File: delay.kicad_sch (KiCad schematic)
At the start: 43 parts, among them Q1301 Q_NPN_BEC, Q1302 Q_NPN_BEC, Q1303 Q_NPN_BEC, Q1304 Q_NPN_BEC, U1301 TL072, U1302 MCP6002, U1303 L78L05_SOT89

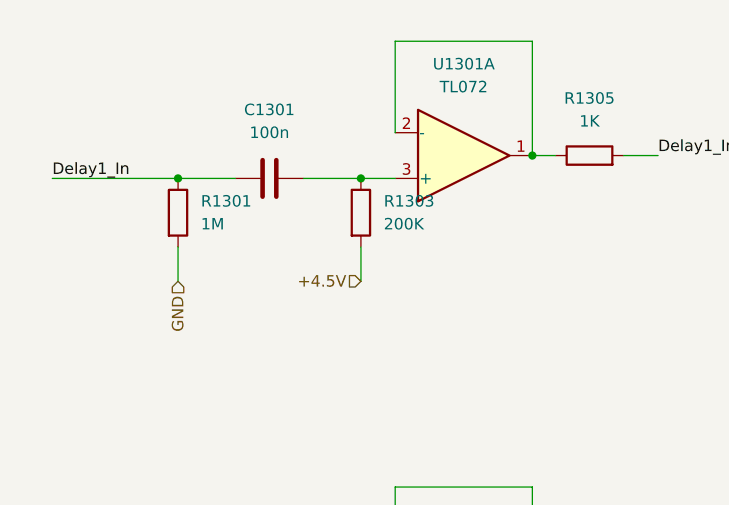
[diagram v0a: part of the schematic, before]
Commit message: Delay layout done
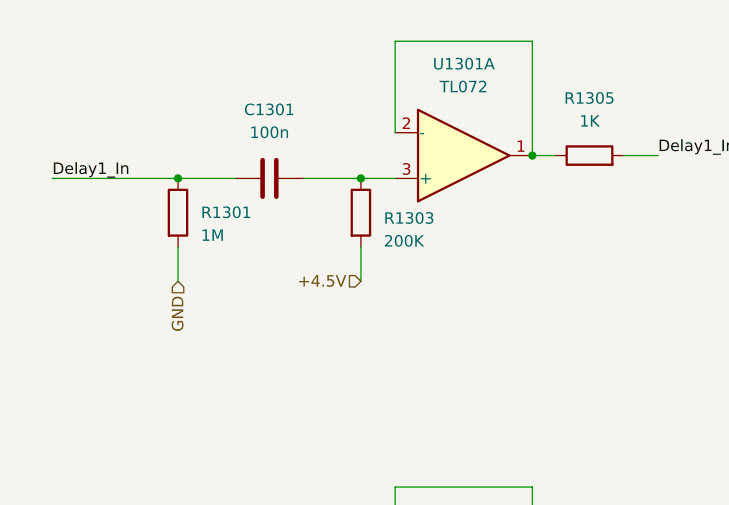
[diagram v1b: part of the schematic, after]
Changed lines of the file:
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@@
   )
   (symbol (lib_id "Device:R") (at 30.48 34.29 0) (unit 1)
-    (in_bom yes) (on_board yes) (fields_autoplaced)
-    (property "Reference" "R1301" (id 0) (at 33.02 33.0199 0)
-      (effects (font (size 1.27 1.27)) (justify left))
-    )
-    (property "Value" "1M" (id 1) (at 33.02 35.5599 0)
+    (in_bom yes) (on_board yes)
+    (property "Reference" "R1301" (id 0) (at 33.02 34.29 0)
+      (effects (font (size 1.27 1.27)) (justify left))
+    )
+    (property "Value" "1M" (id 1) (at 33.02 36.83 0)
       (effects (font (size 1.27 1.27)) (justify left))
     )
@@
   )
   (symbol (lib_id "Device:R") (at 50.8 34.29 0) (unit 1)
-    (in_bom yes) (on_board yes) (fields_autoplaced)
-    (property "Reference" "R1303" (id 0) (at 53.34 33.0199 0)
-      (effects (font (size 1.27 1.27)) (justify left))
-    )
-    (property "Value" "200K" (id 1) (at 53.34 35.5599 0)
-      (effects (font (size 1.27 1.27)) (justify left))
-    )
+    (in_bom yes) (on_board yes)
+    (property "Reference" "R1303" (id 0) (at 53.34 34.925 0)
+      (effects (font (size 1.27 1.27)) (justify left))
+    )
+    (property "Value" "200K" (id 1) (at 53.34 37.465 0)
+      (effects (font (size 1.27 1.27)) (justify left))
+    )

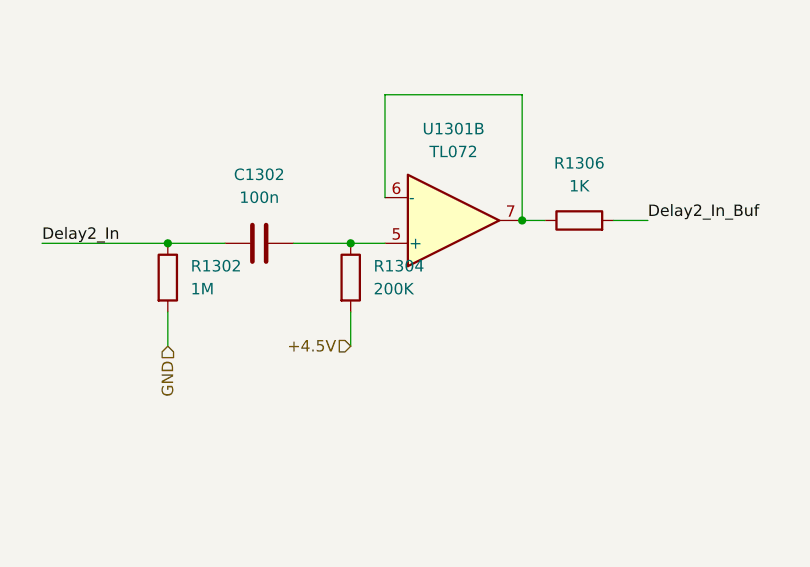
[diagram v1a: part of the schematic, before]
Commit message: Mixer/Crossfader schem capture done
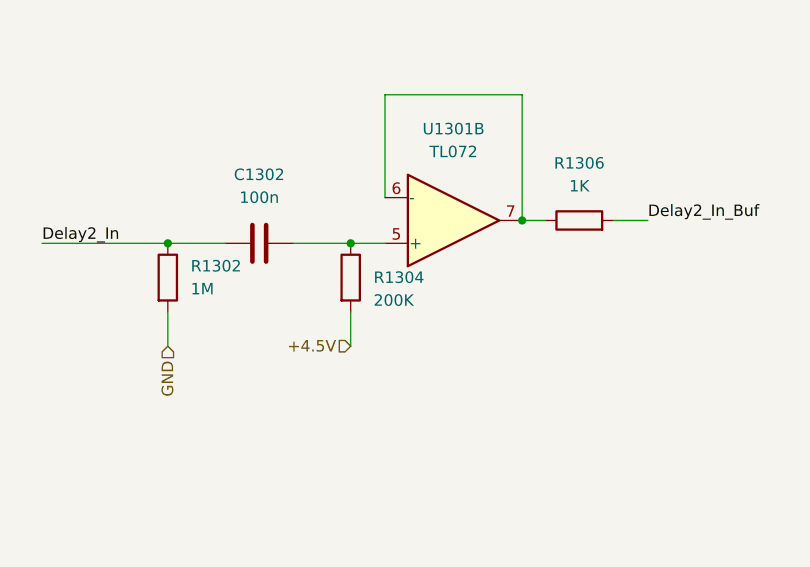
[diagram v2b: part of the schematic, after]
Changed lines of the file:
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@@
   )
   (symbol (lib_id "Device:R") (at 50.8 85.09 0) (unit 1)
-    (in_bom yes) (on_board yes) (fields_autoplaced)
-    (property "Reference" "R1304" (id 0) (at 53.34 83.8199 0)
+    (in_bom yes) (on_board yes)
+    (property "Reference" "R1304" (id 0) (at 53.34 85.09 0)
       (effects (font (size 1.27 1.27)) (justify left))
     )
-    (property "Value" "200K" (id 1) (at 53.34 86.3599 0)
+    (property "Value" "200K" (id 1) (at 53.34 87.63 0)
       (effects (font (size 1.27 1.27)) (justify left))
     )

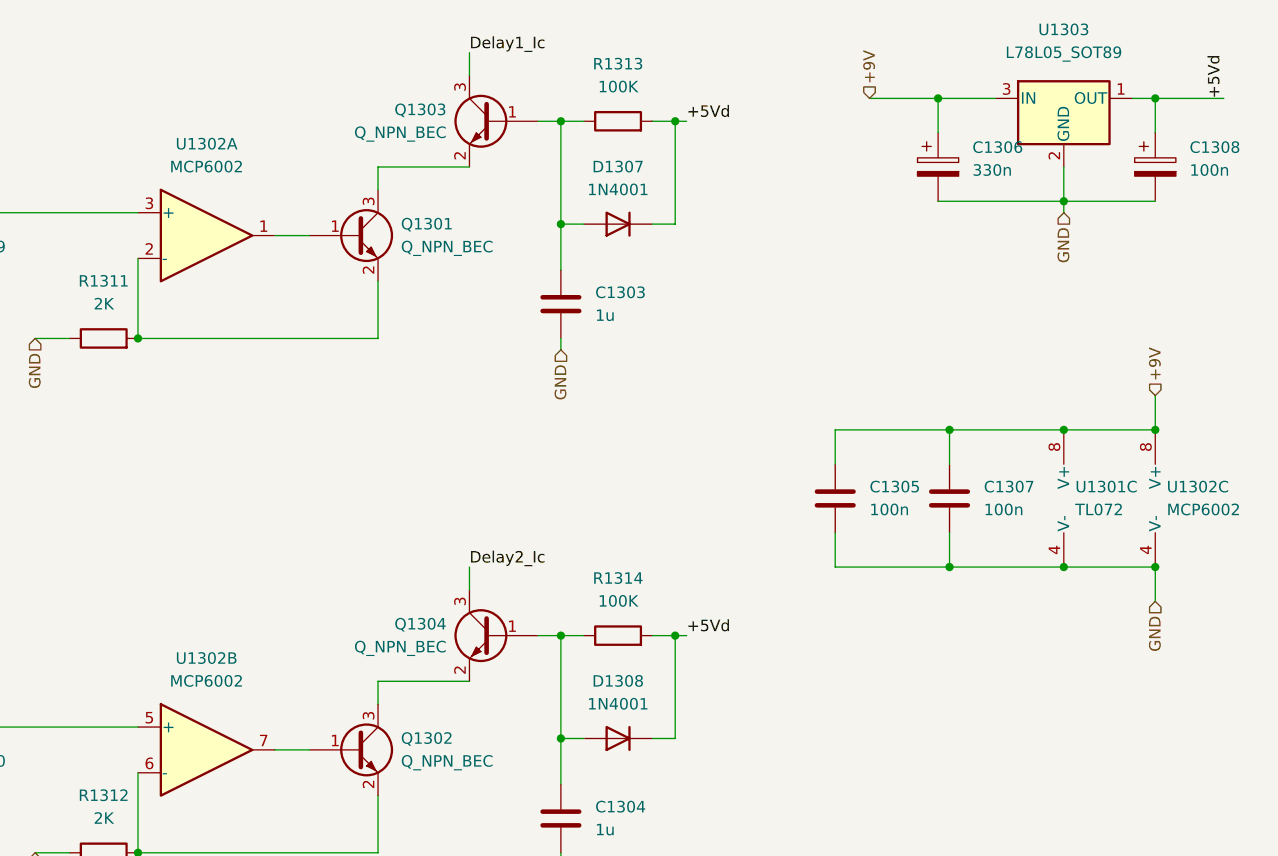
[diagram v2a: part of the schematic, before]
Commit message: LFO schem capture done / replace r2r opamps
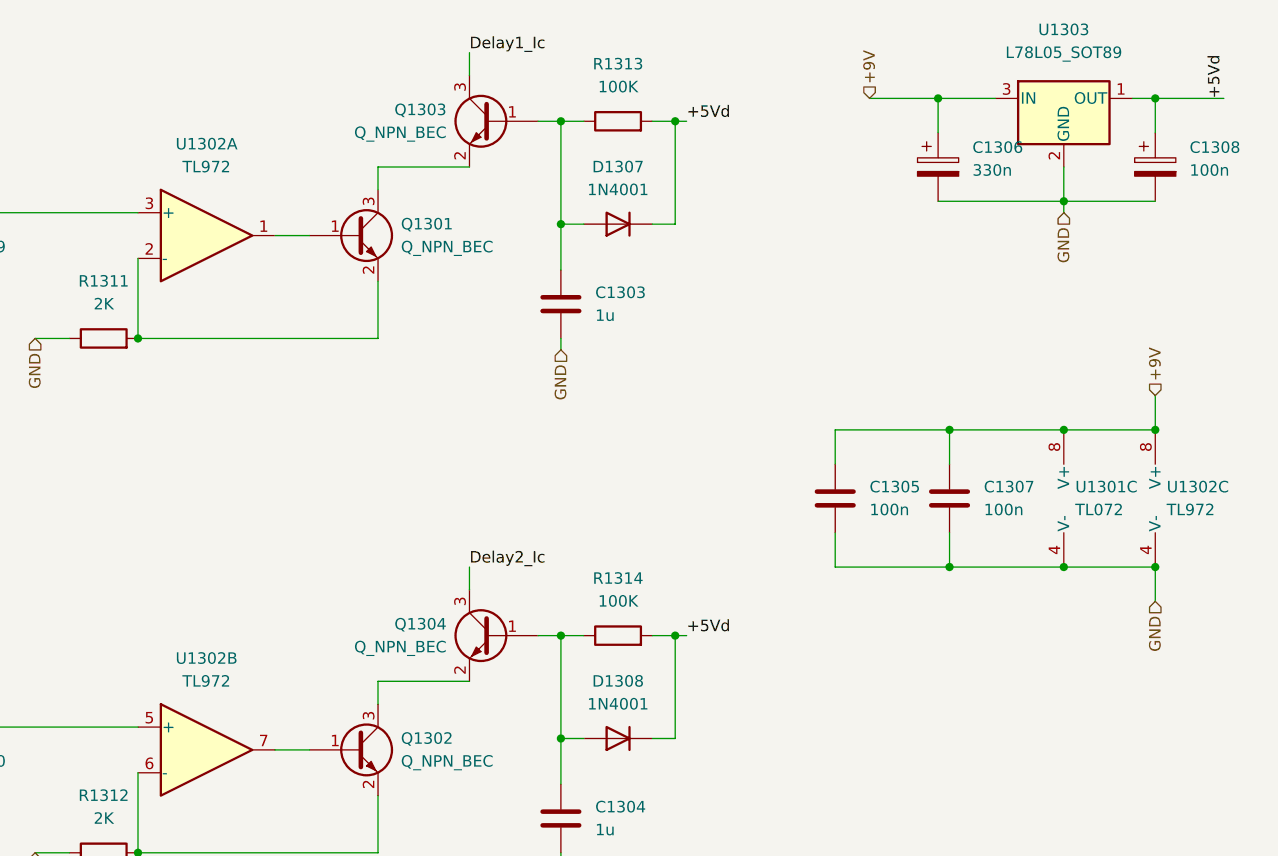
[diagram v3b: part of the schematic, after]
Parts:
- U1302: value MCP6002 -> TL972
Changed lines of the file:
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@@
     (in_bom yes) (on_board yes) (fields_autoplaced)
     (property "Reference" "U1302" (id 0) (at 168.91 26.67 0))
-    (property "Value" "MCP6002" (id 1) (at 168.91 29.21 0))
+    (property "Value" "TL972" (id 1) (at 168.91 29.21 0))
     (property "Footprint" "Package_SO:SOIC-8_3.9x4.9mm_P1.27mm" (id 2) (at 168.91 36.83 0)
       (effects (font (size 1.27 1.27)) hide)
@@
       (effects (font (size 1.27 1.27)) (justify left))
     )
-    (property "Value" "MCP6002" (id 1) (at 275.59 67.3099 0)
+    (property "Value" "TL972" (id 1) (at 275.59 67.3099 0)
       (effects (font (size 1.27 1.27)) (justify left))
     )
@@
     (in_bom yes) (on_board yes) (fields_autoplaced)
     (property "Reference" "U1302" (id 0) (at 168.91 83.82 0))
-    (property "Value" "MCP6002" (id 1) (at 168.91 86.36 0))
+    (property "Value" "TL972" (id 1) (at 168.91 86.36 0))
     (property "Footprint" "Package_SO:SOIC-8_3.9x4.9mm_P1.27mm" (id 2) (at 168.91 93.98 0)
       (effects (font (size 1.27 1.27)) hide)

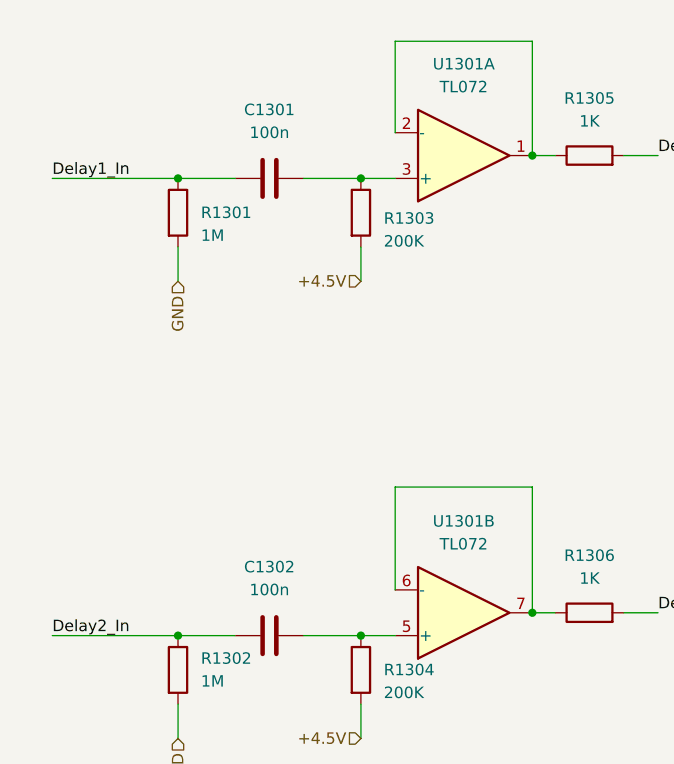
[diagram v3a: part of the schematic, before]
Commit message: Increase the size of dc blocking caps
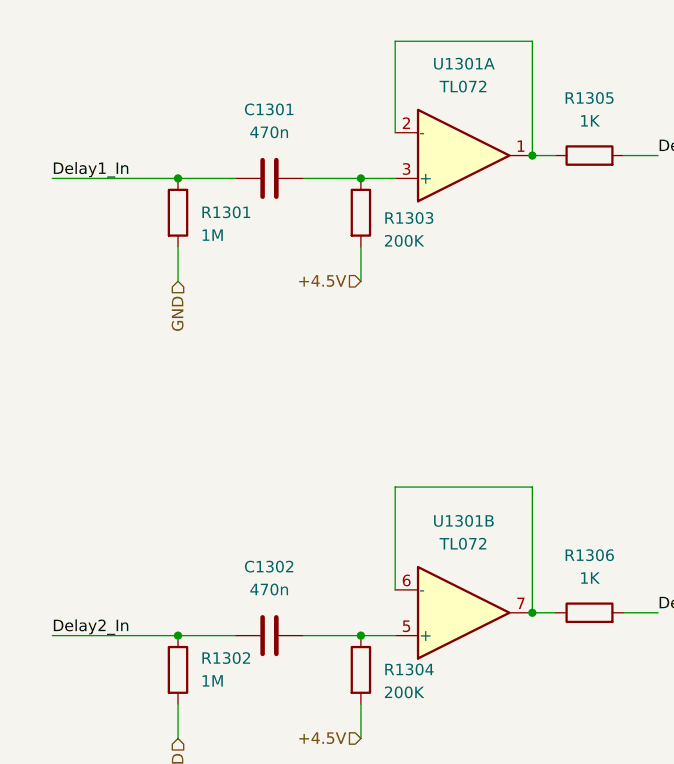
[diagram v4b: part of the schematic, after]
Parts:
- C1301, C1302: value 100n -> 470n; footprint Capacitor_SMD:C_0603_1608Metric_Pad1.08x0.95mm_HandSolder -> Capacitor_SMD:C_0805_2012Metric_Pad1.18x1.45mm_HandSolder
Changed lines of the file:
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@@
+    (pin "2")
+  )
+  (symbol (lib_id "Device:C") (at 40.64 81.28 90) (unit 1)
+    (in_bom yes) (on_board yes) (fields_autoplaced)
+    (property "Reference" "C1302" (id 0) (at 40.64 73.66 90))
+    (property "Value" "470n" (id 1) (at 40.64 76.2 90))
+    (property "Footprint" "Capacitor_SMD:C_0805_2012Metric_Pad1.18x1.45mm_HandSolder" (id 2) (at 44.45 80.3148 0)
+      (effects (font (size 1.27 1.27)) hide)
+    )
+    (property "Datasheet" "~" (id 3) (at 40.64 81.28 0)
+      (effects (font (size 1.27 1.27)) hide)
+    )
+    (pin "1")
     (pin "2")
   )
@@
     (pin "2")
   )
-  (symbol (lib_id "Device:C") (at 40.64 81.28 90) (unit 1)
-    (in_bom yes) (on_board yes) (fields_autoplaced)
-    (property "Reference" "C1302" (id 0) (at 40.64 73.66 90))
-    (property "Value" "100n" (id 1) (at 40.64 76.2 90))
-    (property "Footprint" "Capacitor_SMD:C_0603_1608Metric_Pad1.08x0.95mm_HandSolder" (id 2) (at 44.45 80.3148 0)
-      (effects (font (size 1.27 1.27)) hide)
-    )
-    (property "Datasheet" "~" (id 3) (at 40.64 81.28 0)
-      (effects (font (size 1.27 1.27)) hide)
-    )
-    (pin "1")
-    (pin "2")
-  )
   (symbol (lib_id "Device:R") (at 138.43 39.37 0) (unit 1)
     (in_bom yes) (on_board yes) (fields_autoplaced)
@@
     )
     (property "Datasheet" "~" (id 3) (at 138.43 39.37 0)
+      (effects (font (size 1.27 1.27)) hide)
+    )
+    (pin "1")
+    (pin "2")
+  )
+  (symbol (lib_id "Device:C") (at 40.64 30.48 90) (unit 1)
+    (in_bom yes) (on_board yes) (fields_autoplaced)
+    (property "Reference" "C1301" (id 0) (at 40.64 22.86 90))
+    (property "Value" "470n" (id 1) (at 40.64 25.4 90))
+    (property "Footprint" "Capacitor_SMD:C_0805_2012Metric_Pad1.18x1.45mm_HandSolder" (id 2) (at 44.45 29.5148 0)
+      (effects (font (size 1.27 1.27)) hide)
+    )
+    (property "Datasheet" "~" (id 3) (at 40.64 30.48 0)
       (effects (font (size 1.27 1.27)) hide)
     )
@@
       (effects (font (size 1.27 1.27)) hide)
     )
-    (pin "1")
-    (pin "2")
-  )
-  (symbol (lib_id "Device:C") (at 40.64 30.48 90) (unit 1)
-    (in_bom yes) (on_board yes) (fields_autoplaced)
-    (property "Reference" "C1301" (id 0) (at 40.64 22.86 90))
-    (property "Value" "100n" (id 1) (at 40.64 25.4 90))
-    (property "Footprint" "Capacitor_SMD:C_0603_1608Metric_Pad1.08x0.95mm_HandSolder" (id 2) (at 44.45 29.5148 0)
-      (effects (font (size 1.27 1.27)) hide)
-    )
-    (property "Datasheet" "~" (id 3) (at 40.64 30.48 0)
-      (effects (font (size 1.27 1.27)) hide)
-    )

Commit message: PSU schem update
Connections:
- net +9V: no longer C1306.1, U1303.3 (IN)
- new net +9Vd: C1306.1, U1303.3 (IN)
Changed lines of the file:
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@@
     (effects (font (size 1.27 1.27)) (justify right))
   )
-  (hierarchical_label "+9V" (shape input) (at 242.57 21.59 90)
+  (hierarchical_label "+9Vd" (shape input) (at 242.57 21.59 90)
     (effects (font (size 1.27 1.27)) (justify left))
   )

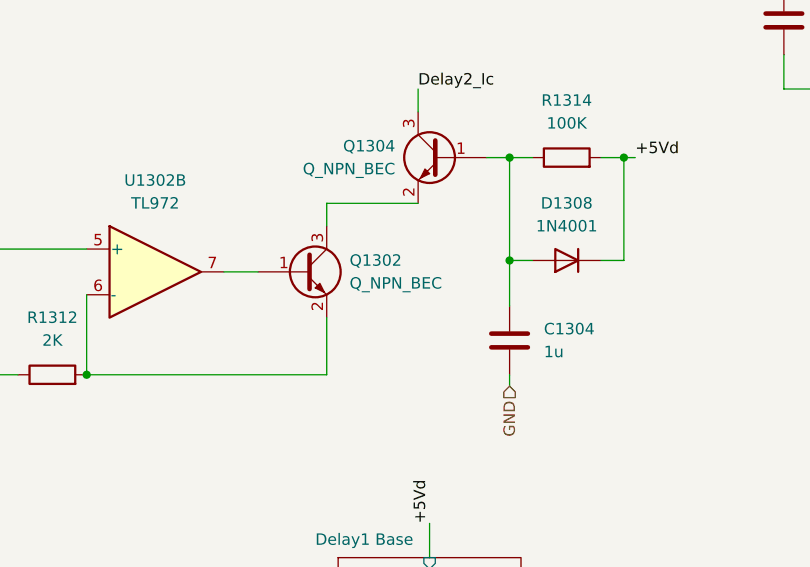
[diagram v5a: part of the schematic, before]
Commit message: Jacks schem done
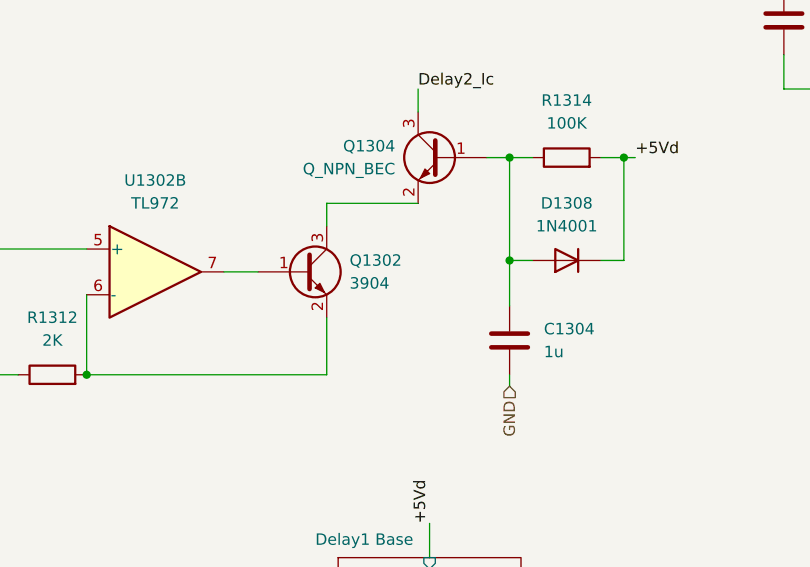
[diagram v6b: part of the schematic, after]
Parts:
- Q1302: value Q_NPN_BEC -> 3904
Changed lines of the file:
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@@
       (effects (font (size 1.27 1.27)) (justify left))
     )
-    (property "Value" "Q_NPN_BEC" (id 1) (at 190.5 95.2499 0)
+    (property "Value" "3904" (id 1) (at 190.5 95.2499 0)
       (effects (font (size 1.27 1.27)) (justify left))
     )

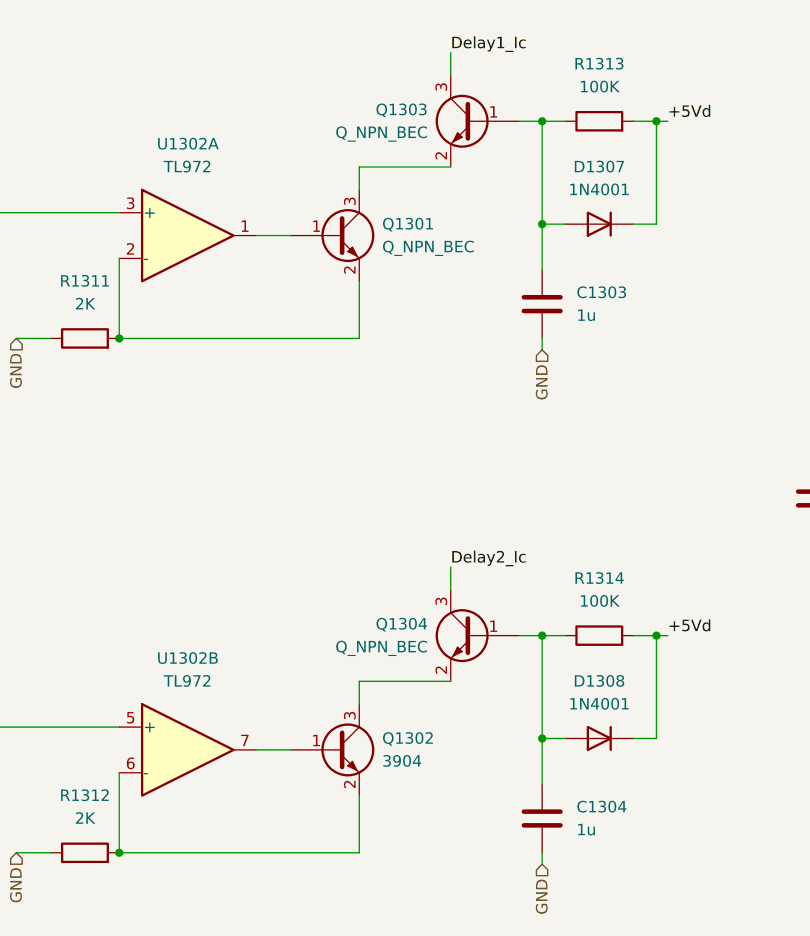
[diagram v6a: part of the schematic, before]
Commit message: Add JLC parts numbers
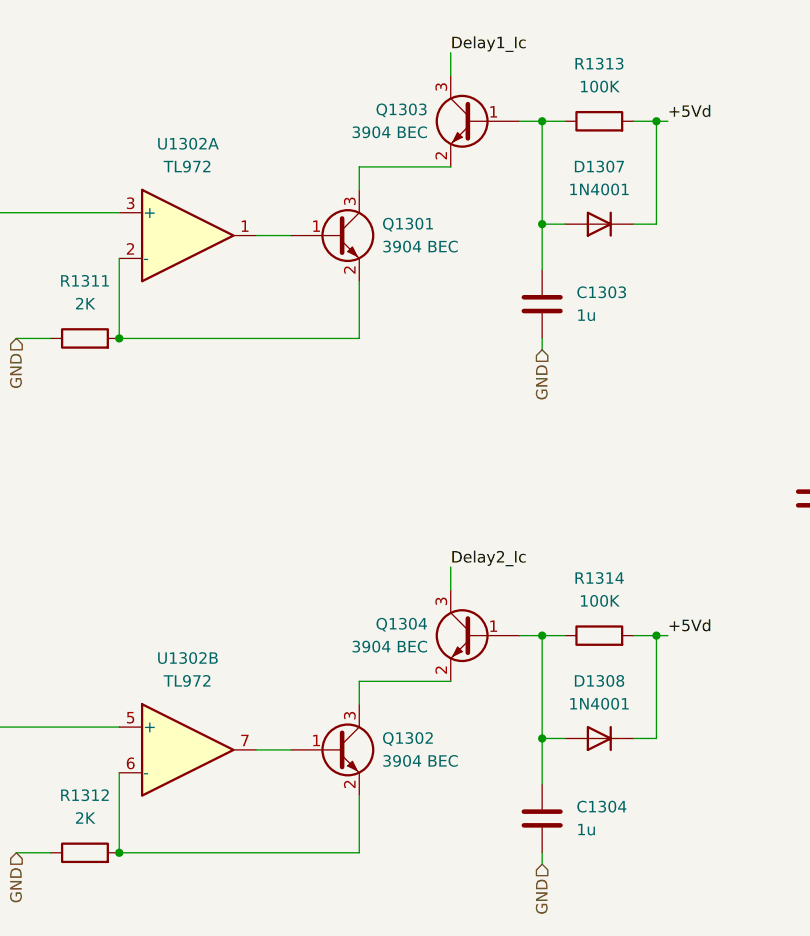
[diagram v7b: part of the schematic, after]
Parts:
- C1301, C1302: LCSC (none) -> C651004; Role (none) -> audio-coupling
- C1303, C1304: LCSC (none) -> C59302; Role (none) -> cv-filter
- C1305, C1307: LCSC (none) -> C497032; Role (none) -> ic-bypass
- C1306: LCSC (none) -> C264238; Role (none) -> psu-filter
- C1308: LCSC (none) -> C271438; Role (none) -> psu-filter
- D1301, D1302, D1303, D1304, D1305, D1306: LCSC (none) -> C20936
- D1307, D1308: LCSC (none) -> C122841
- Q1301, Q1303, Q1304: value Q_NPN_BEC -> 3904 BEC; LCSC (none) -> C20526
- Q1302: value 3904 -> 3904 BEC; LCSC (none) -> C20526
- R1301, R1302: LCSC (none) -> C234360
- R1303, R1304, R1307, R1308: LCSC (none) -> C203392
- R1305, R1306: LCSC (none) -> C2907002
- R1309, R1310: LCSC (none) -> C2907063
- R1311, R1312: LCSC (none) -> C2907022
- R1313, R1314: LCSC (none) -> C14675
- U1301: LCSC (none) -> C67473
- U1302: LCSC (none) -> C46127
- U1303: LCSC (none) -> C347258
